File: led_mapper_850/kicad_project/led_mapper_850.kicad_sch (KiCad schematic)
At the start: 0 parts

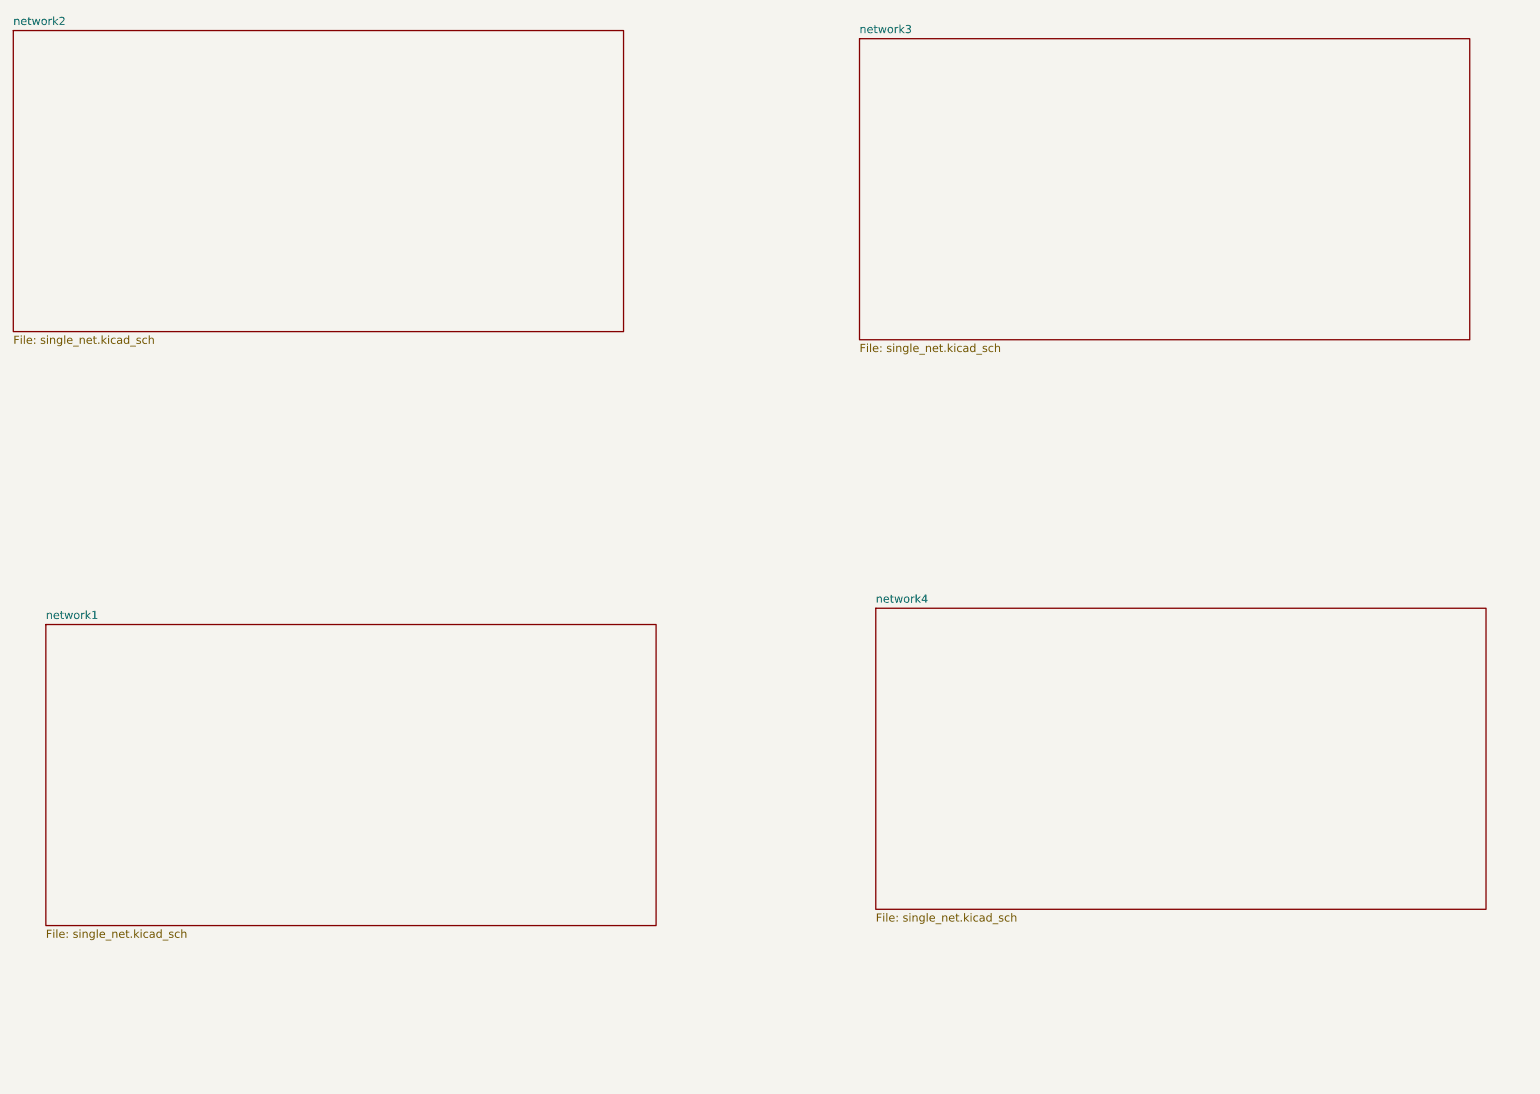
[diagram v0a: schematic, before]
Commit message: use single connector
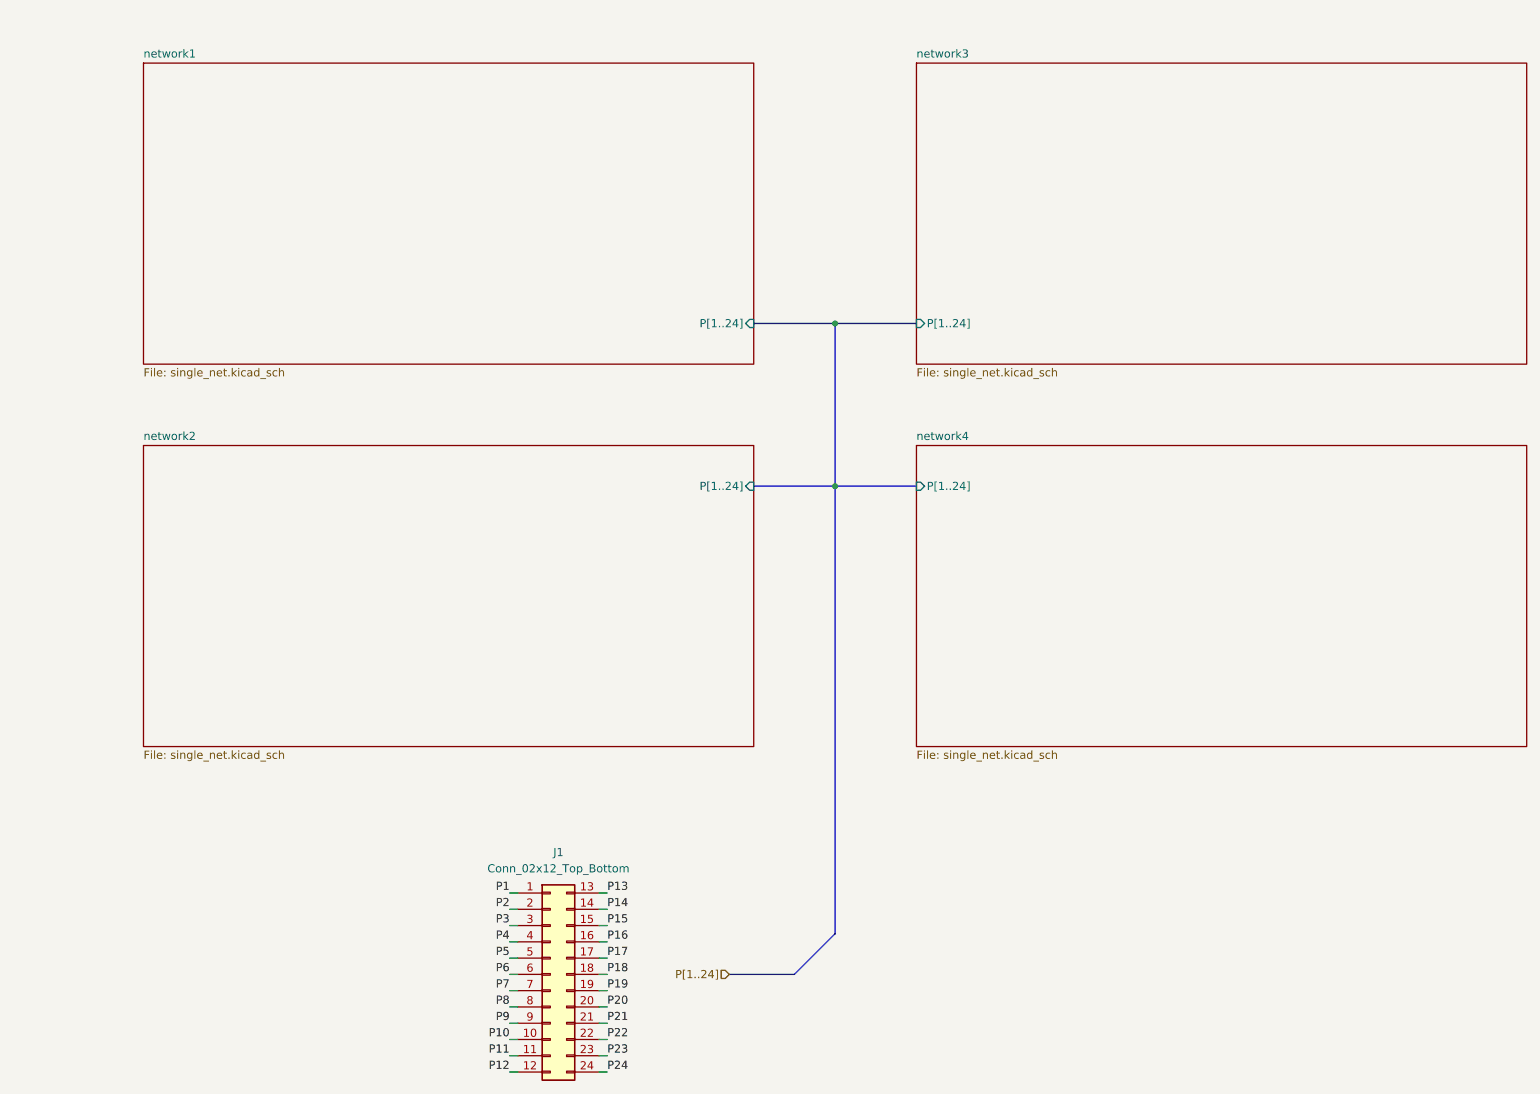
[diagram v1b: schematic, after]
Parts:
- added J1: Conn_02x12_Top_Bottom, ccatlib:PinSocket_2x12_P2.54mm_Vertical_SMD_custom, symbol Connector_Generic:Conn_02x12_Top_Bottom
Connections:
- new net P1: J1.1 (Pin_1)
- new net P10: J1.10 (Pin_10)
- new net P11: J1.11 (Pin_11)
- new net P12: J1.12 (Pin_12)
- new net P13: J1.13 (Pin_13)
- new net P14: J1.14 (Pin_14)
- new net P15: J1.15 (Pin_15)
- new net P16: J1.16 (Pin_16)
- new net P17: J1.17 (Pin_17)
- new net P18: J1.18 (Pin_18)
- new net P19: J1.19 (Pin_19)
- new net P2: J1.2 (Pin_2)
- new net P20: J1.20 (Pin_20)
- new net P21: J1.21 (Pin_21)
- new net P22: J1.22 (Pin_22)
- new net P23: J1.23 (Pin_23)
- new net P24: J1.24 (Pin_24)
- new net P3: J1.3 (Pin_3)
- new net P4: J1.4 (Pin_4)
- new net P5: J1.5 (Pin_5)
- new net P6: J1.6 (Pin_6)
- new net P7: J1.7 (Pin_7)
- new net P8: J1.8 (Pin_8)
- new net P9: J1.9 (Pin_9)
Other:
- sheet network1 ports: added P[1..24]; removed none
- sheet network2 ports: added P[1..24]; removed none
- sheet network3 ports: added P[1..24]; removed none
- sheet network4 ports: added P[1..24]; removed none
